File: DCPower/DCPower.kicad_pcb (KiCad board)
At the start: 6 copper layers, 80 x 50 mm, 104 parts, among them IC1 LTC4417CUF#PBF, J1 USB_C_Receptacle_USB2.0_14P, J2 XT30, J4 Barrel_Jack_Switch, Q1 DMP4025LSD-13, Q2 DMP4025LSD-13, Q3 DMP4025LSD-13, Q4 DMP4025LSD-13, Q5 DMP4025LSD-13, Q6 2N7002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

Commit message: More Power Path, fixed filter
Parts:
- removed IC1: LTC4417CUF#PBF, UniversalAlexLibrary:QFN50P400X400X80-25N-D
- added C26: 10uF, PCM_JLCPCB:C_1206, F.Cu at (173.6, 75.7)
- added C27: 10uF, PCM_JLCPCB:C_1206, F.Cu at (173.6, 78.2)
- added C28: 10uF, PCM_JLCPCB:C_1206, F.Cu at (184.5, 67.2)
- added C29: 10uF, PCM_JLCPCB:C_1206, F.Cu at (184.5, 64.8)
- added C30: 10uF, PCM_JLCPCB:C_1206, F.Cu at (184.5, 62.2)
- added C31: 2.2uF, PCM_JLCPCB:C_0805, F.Cu at (184.4, 69.5)
- added C32: 4.7uF, PCM_JLCPCB:C_1206, F.Cu at (184.5, 59.8)
- added U5: LTC4417CUF#PBF, UniversalAlexLibrary:QFN50P400X400X80-25N-D, F.Cu at (180.6, 88.7)
- moved C14 107.0 mm to (177.8, 59.7), turned to 180 degrees
- moved C7 103.2 mm to (175.5, 69.8)
- moved R36 95.6 mm to (176.6, 89.3)
- moved L1 93.0 mm to (172.0, 62.2), turned to 90 degrees
- moved R10 92.2 mm to (183.1, 93.2)
- moved R11 90.1 mm to (183.1, 92.0)
- moved R4 87.0 mm to (177.9, 93.2)
- moved R13 86.7 mm to (184.5, 88.0), turned to 180 degrees
- moved R14 86.6 mm to (184.8, 89.4), turned to 180 degrees
- moved R7 86.3 mm to (180.5, 94.5)
- moved R15 85.9 mm to (184.5, 90.8), turned to 180 degrees
- moved R5 85.1 mm to (177.9, 92.0)
- moved R8 84.6 mm to (180.5, 93.2)
- moved R12 80.6 mm to (177.2, 86.0), turned to 90 degrees
- moved Q1 80.1 mm to (166.4, 84.5), turned to 90 degrees
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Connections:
- C1 pad 1: +VBUS_PD -> Net-(Q1-D1_1)
- C2 pad 1: Net-(IC1-V3) -> +VBUS_PD
- D5 pad 1: Net-(IC1-V3) -> Net-(Q1-D1_1)
- Q1 pad 7: +VBUS_PD -> Net-(Q1-D1_1)
- Q1 pad 8: +VBUS_PD -> Net-(Q1-D1_1)
- Q3 pad 7: Net-(IC1-V3) -> +VBUS_PD
- Q3 pad 8: Net-(IC1-V3) -> +VBUS_PD
- Q8 pad 2: Net-(IC1-V3) -> Net-(Q1-D1_1)
- R12 pad 1: Net-(IC1-V3) -> +VBUS_PD
- R37 pad 1: +5V_USB -> +VBUS_SAFE
- R6 pad 1: +VBUS_PD -> Net-(Q1-D1_1)
- U2 pad 22: GND -> Net-(U2-GND-Pad22)
- U2 pad 25: GND -> Net-(U2-GND-Pad22)
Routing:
- net +VBUS_PD: track 43.4 -> 82.2 mm, vias 3 -> 5
- net Net-(Q3-S1): track 0.00 -> 34.0 mm, vias 0 -> 2
- net Net-(Q2-D1_1): track 0.00 -> 30.0 mm, vias 0 -> 2
- net Net-(Q3-G1): track 0.00 -> 29.8 mm, vias 0 -> 2
- net Net-(Q1-S1): track 0.00 -> 29.3 mm
- net Net-(Q2-S1): track 0.00 -> 27.5 mm, vias 0 -> 2
- net Net-(Q1-G1): track 0.00 -> 25.1 mm
- net Net-(Q2-G1): track 0.00 -> 23.5 mm, vias 0 -> 2
- net Net-(Q1-D1_1): track 0.00 -> 20.2 mm, vias 0 -> 2
- net Net-(U5-UV2): track 0.00 -> 18.2 mm, vias 0 -> 2
- net Net-(Q1-D2_1): track 0.00 -> 17.5 mm, vias 0 -> 2
- net Net-(U5-UV3): track 0.00 -> 15.5 mm, vias 0 -> 2
- net Net-(J1-SHIELD): track 0.00 -> 13.9 mm
- net Net-(U5-UV1): track 0.00 -> 9.11 mm
- net GND: track 12.7 -> 21.2 mm, vias 1 -> 10
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- added copper zone on F.Cu, net +VBUS_PD
- added copper zone on F.Cu, net +V_MAIN
- added copper zone on F.Cu, net Net-(Q1-D1_1)
- added copper zone on F.Cu, net Net-(Q1-D2_1)
- added copper zone on F.Cu, net Net-(Q1-S1)
- added copper zone on F.Cu, net Net-(Q2-D1_1)
- added copper zone on F.Cu, net Net-(U5-EN)

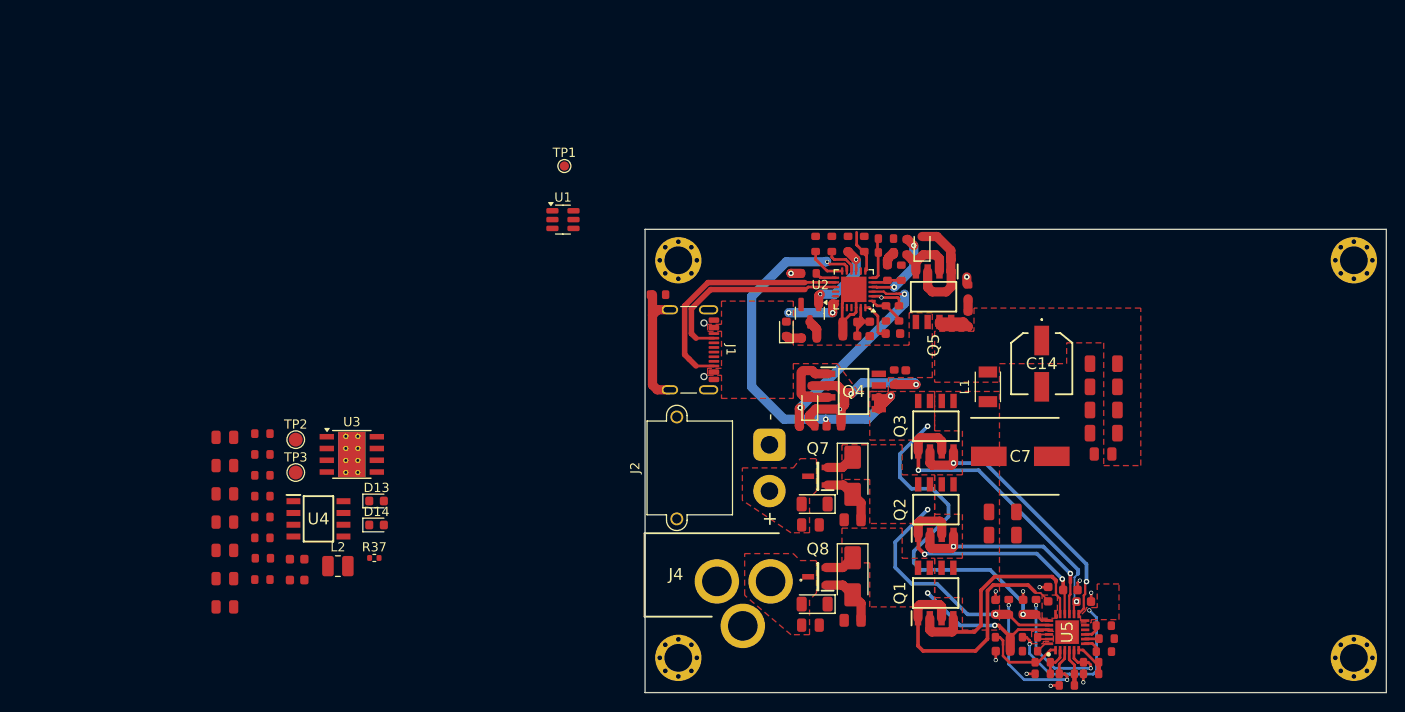
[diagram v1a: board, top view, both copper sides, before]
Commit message: Forked into Simple 1 input version
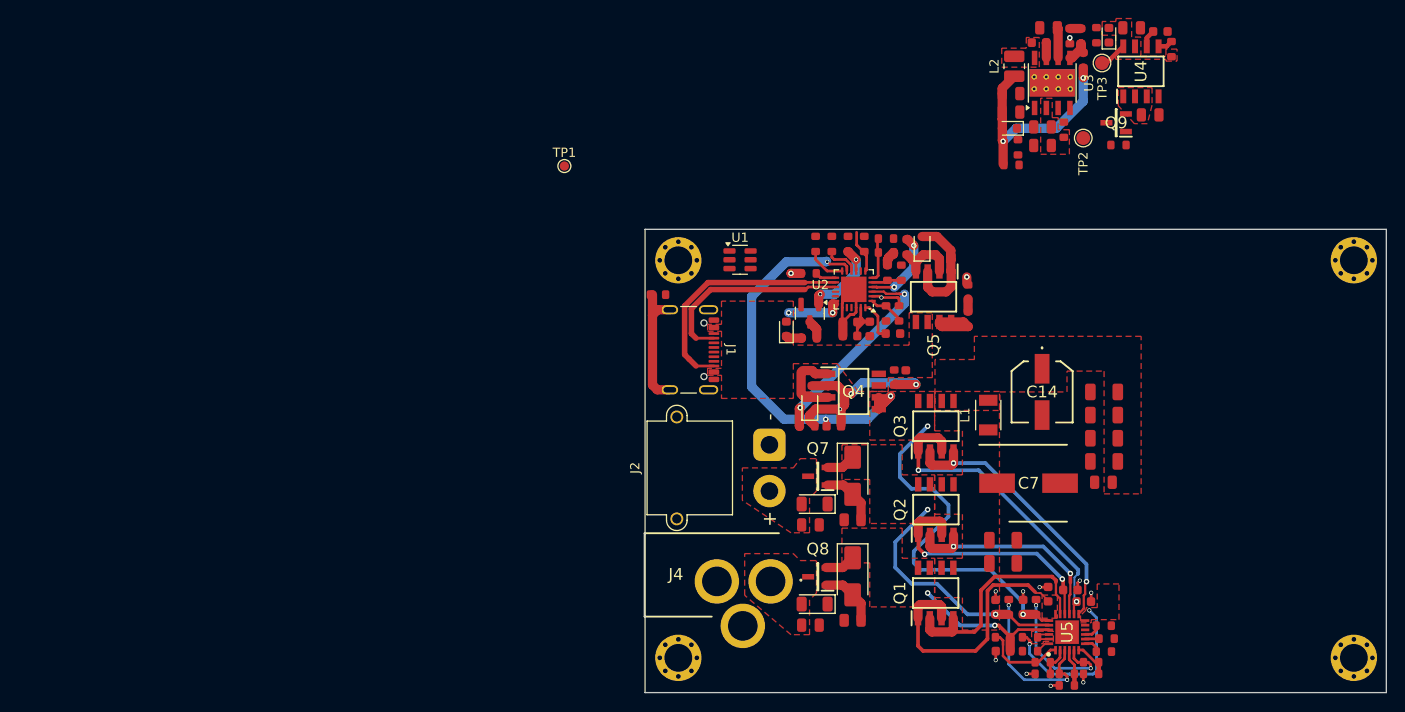
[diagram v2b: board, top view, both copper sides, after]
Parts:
- added Q9: SQ2319CES-T1_GE3, SwiftModules:SOT95P237X112-3N, F.Cu at (185.8, 33.7)
- R37: value 10k -> 10kΩ; footprint Resistor_SMD:R_0402_1005Metric -> PCM_JLCPCB:R_0603
- moved C23 114.5 mm to (187.5, 23.5)
- moved C24 113.1 mm to (189.5, 32.9)
- moved R43 111.4 mm to (191.8, 25.8), turned to 90 degrees
- moved C25 110.4 mm to (190.6, 23.9), turned to 180 degrees
- moved R44 106.2 mm to (183.7, 24.3), turned to 90 degrees
- moved C22 105.3 mm to (178.5, 23.5), turned to 180 degrees
- moved R42 101.4 mm to (180.8, 24.4), turned to -90 degrees
- moved U4 101.1 mm to (188.5, 28.2), turned to 90 degrees
- moved R39 99.2 mm to (182.0, 24.4), turned to 90 degrees
- moved R69 99.2 mm to (180.2, 34.5), turned to 90 degrees
- moved TP3 97.6 mm to (184.3, 27.3), turned to 90 degrees
- moved C17 97.6 mm to (177.5, 25.1), turned to 180 degrees
- moved R38 97.3 mm to (182.3, 27.0), turned to 90 degrees
- moved C21 95.7 mm to (174.5, 32.6)
- moved C19 95.5 mm to (177.9, 34.2), turned to 180 degrees
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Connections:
- C26 pad 1: Net-(Q1-D2_1) -> Net-(C26-Pad1)
- C27 pad 1: Net-(Q1-D2_1) -> Net-(C26-Pad1)
- C7 pad 1: Net-(Q1-D2_1) -> Net-(C26-Pad1)
- L1 pad 1: Net-(Q1-D2_1) -> Net-(C26-Pad1)
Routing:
- net Net-(D13-A): track 0.00 -> 24.1 mm, vias 0 -> 2
- net Net-(U3-VCC): track 0.00 -> 3.29 mm
- net Net-(U3-FB): track 0.00 -> 3.22 mm
- net +3V3: track 0.00 -> 3.04 mm
- net Net-(U4-CDELAY): track 0.00 -> 1.88 mm
- net Net-(U3-BOOT): track 0.00 -> 1.66 mm
- net Net-(U4-PWRGD): track 0.00 -> 1.61 mm
- net Net-(R39-Pad2): track 0.00 -> 1.20 mm
- net GND: track 21.2 -> 21.9 mm, vias 10 -> 11
- added copper zone on F.Cu, net +3V3
- added copper zone on F.Cu, net +5V
- added copper zone on F.Cu, net Net-(U3-SW)
